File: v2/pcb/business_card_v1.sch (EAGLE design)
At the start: 31 parts, among them SW1 SPST_TACT-KMR2

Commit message: get the led layout right
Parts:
- removed ATTINY: ATTINY45-20X, _hhn_attiny25_45_85:ATTINY45-20X
- removed ISP1: AVRISP-6, adafruit:AVRISP-6
- added IC1: (no value), atmel_tiny24-44-84tiny48-88mega48-88-168-328:ATTINY24/44/84-MU
- added LED21, LED22, LED23, LED24, LED25, LED26, LED27, LED28, LED29, LED30, LED31, LED32, LED33, LED34, LED35, LED36, LED37, LED38, LED39, LED40, LED41, LED42, LED43, LED44, LED45, LED46, LED47, LED48, LED49, LED50, LED51, LED52, LED53, LED54, LED55, LED56: (no value), led:LEDCHIPLED_0805
- added R7, R8, R9: 150, resistor:R-US_R0603
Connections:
- removed net PIN1: ATTINY.PB1, ISP1.MISO, R2.1
- removed net PIN2: ATTINY.PB2, ISP1.SCK, R3.1
- removed net PIN3: ATTINY.PB3, R6.1
- removed net PIN4: ATTINY.PB4, R5.1
- new net N$10: R4.1
- new net N$11: R5.1
- new net N$15: LED10.C, LED11.C, LED12.C, LED13.C, LED14.C, LED15.A, LED23.A, LED31.A, LED39.A, LED47.A, LED55.A, LED7.A, LED8.C, LED9.C, R8.2
- new net N$2: LED10.A, LED18.A, LED2.A, LED26.A, LED34.A, LED42.A, LED43.C, LED44.C, LED45.C, LED46.C, LED47.C, LED48.C, LED49.C, LED50.A, R3.2
- new net N$3: LED11.A, LED19.A, LED27.A, LED3.A, LED35.A, LED36.C, LED37.C, LED38.C, LED39.C, LED40.C, LED41.C, LED42.C, LED43.A, LED51.A, R4.2
- new net N$31: LED14.A, LED15.C, LED16.C, LED17.C, LED18.C, LED19.C, LED20.C, LED21.C, LED22.A, LED30.A, LED38.A, LED46.A, LED54.A, LED6.A, R7.2
- new net N$34: LED13.A, LED21.A, LED22.C, LED23.C, LED24.C, LED25.C, LED26.C, LED27.C, LED28.C, LED29.A, LED37.A, LED45.A, LED5.A, LED53.A, R6.2
- new net N$4: LED12.A, LED20.A, LED28.A, LED29.C, LED30.C, LED31.C, LED32.C, LED33.C, LED34.C, LED35.C, LED36.A, LED4.A, LED44.A, LED52.A, R5.2
- new net N$5: R8.1
- new net N$8: LED1.C, LED16.A, LED2.C, LED24.A, LED3.C, LED32.A, LED4.C, LED40.A, LED48.A, LED5.C, LED56.A, LED6.C, LED7.C, LED8.A, R9.2
- net +5V: no longer ATTINY.VCC, ISP1.VCC
- net GND: no longer ATTINY.GND, ISP1.GND
- net N$1: now also LED17.A, LED25.A, LED33.A, LED41.A, LED49.A, LED50.C, LED51.C, LED52.C, LED53.C, LED54.C, LED55.C, LED56.C, LED9.A; no longer LED11.A, LED16.A, LED17.C, LED18.C, LED19.C, LED20.C, LED6.A
- net N$12: now also R6.1; no longer LED10.C, LED11.C, LED12.C, LED13.A, LED18.A, LED3.A, LED8.A, LED9.C, R4.2
- net N$13: now also R7.1; no longer LED12.A, LED13.C, LED14.C, LED15.C, LED16.C, LED17.A, LED2.A, LED7.A, R3.2
- net N$6: now also R9.1; no longer LED1.C, LED10.A, LED15.A, LED2.C, LED20.A, LED3.C, LED4.C, LED5.A, R6.2
- net N$9: now also R3.1; no longer LED14.A, LED19.A, LED4.A, LED5.C, LED6.C, LED7.C, LED8.C, LED9.A, R5.2
- net PIN0: now also R2.1; no longer ATTINY.PB0, ISP1.MOSI, R4.1
- net RESET: no longer ATTINY.NRES/PB5, ISP1.RST
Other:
- moved on the sheet: C1, JP1, LED1, LED10, LED11, LED12, LED13, LED14, LED15, LED16, LED17, LED18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

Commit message: update pcb and schematic
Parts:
- IC1: device atmel_tiny24-44-84tiny48-88mega48-88-168-328:ATTINY24/44/84-MU -> atmel_tiny24-44-84tiny48-88mega48-88-168-328:ATTINY24/44/84-SSU
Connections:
- net +5V renamed UCC
- removed net N$10: R4.1
- removed net N$11: R5.1
- removed net N$12: R6.1
- removed net N$13: R7.1
- removed net N$5: R8.1
- removed net N$6: R9.1
- removed net N$9: R3.1
- new net PIN1: IC1IC.PA1(ADC1/AIN0/PCINT1), R3.1
- new net PIN2: IC1IC.PA2(ADC2/AIN1/PCINT2), R4.1
- new net PIN3: IC1IC.PA3(ADC3/T0/PCINT3), R5.1
- new net PIN4: IC1IC.PA4(ADC4/USCK/SCL/T1/PCINT4), R6.1
- new net PIN5: IC1IC.PA5(ADC5/MISO/DO/OC1B/PCINT5), R7.1
- new net PIN6: IC1IC.PA6(ADC6/MOSI/SDA/OC1A/PCINT6), R8.1
- new net PIN7: IC1IC.PA7(ADC7/ICP/OC0B/PCINT7), R9.1
- net PIN0: now also IC1IC.PA0(ADC0/AREF/PCINT0)
- net RESET: now also IC1IC.PB3(!RESET!/DW/PCINT11)
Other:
- moved on the sheet: C1, IC1

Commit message: business card
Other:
- moved on the sheet: C1, IC1, JP1, LED1, LED10, LED11, LED12, LED13, LED14, LED15, LED16, LED17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

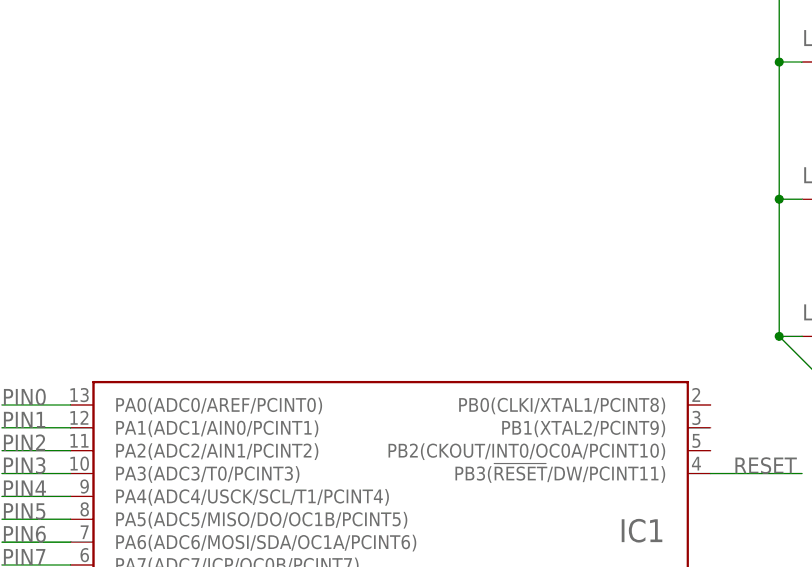
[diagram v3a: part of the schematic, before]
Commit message: get the business card design done, looking for review now
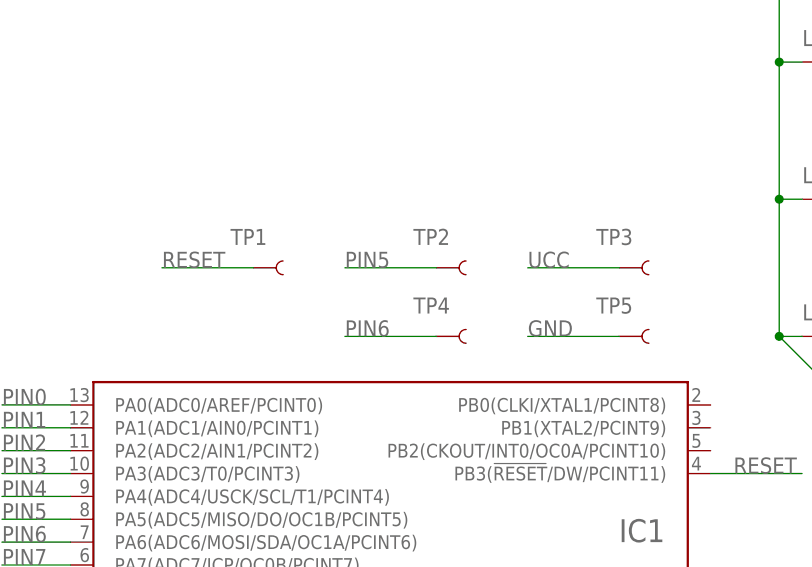
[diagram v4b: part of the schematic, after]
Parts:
- added TP1, TP2, TP3, TP4, TP5: TEST-POINT3X5, SparkFun-Connectors:TEST-POINT3X5
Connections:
- net GND: now also TP5.1
- net PIN5: now also TP2.1
- net PIN6: now also TP4.1
- net RESET: now also TP1.1
- net UCC: now also TP3.1
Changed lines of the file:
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@@
 <layers>
 <layer number="1" name="Top" color="4" fill="1" visible="no" active="no"/>
+<layer number="2" name="Route2" color="1" fill="3" visible="no" active="no"/>
+<layer number="3" name="Route3" color="4" fill="3" visible="no" active="no"/>
+<layer number="4" name="Route4" color="1" fill="4" visible="no" active="no"/>
+<layer number="5" name="Route5" color="4" fill="4" visible="no" active="no"/>
+<layer number="6" name="Route6" color="1" fill="8" visible="no" active="no"/>
+<layer number="7" name="Route7" color="4" fill="8" visible="no" active="no"/>
+<layer number="8" name="Route8" color="1" fill="2" visible="no" active="no"/>
+<layer number="9" name="Route9" color="4" fill="2" visible="no" active="no"/>
+<layer number="10" name="Route10" color="1" fill="7" visible="no" active="no"/>
+<layer number="11" name="Route11" color="4" fill="7" visible="no" active="no"/>
+<layer number="12" name="Route12" color="1" fill="5" visible="no" active="no"/>
+<layer number="13" name="Route13" color="4" fill="5" visible="no" active="no"/>
+<layer number="14" name="Route14" color="1" fill="6" visible="no" active="no"/>
+<layer number="15" name="Route15" color="4" fill="6" visible="no" active="no"/>
 <layer number="16" name="Bottom" color="1" fill="1" visible="no" active="no"/>
 <layer number="17" name="Pads" color="2" fill="1" visible="no" active="no"/>
@@
 <layer number="59" name="tCarbon" color="7" fill="1" visible="no" active="no"/>
 <layer number="60" name="bCarbon" color="7" fill="1" visible="no" active="no"/>
+<layer number="88" name="SimResults" color="9" fill="1" visible="no" active="yes"/>
+<layer number="89" name="SimProbes" color="9" fill="1" visible="no" active="yes"/>
 <layer number="90" name="Modules" color="5" fill="1" visible="yes" active="yes"/>
 <layer number="91" name="Nets" color="2" fill="1" visible="yes" active="yes"/>
@@
 <layer number="112" name="tSilk" color="7" fill="1" visible="no" active="yes"/>
 <layer number="113" name="ReferenceLS" color="7" fill="1" visible="no" active="no"/>
+<layer number="114" name="Badge_Outline" color="7" fill="1" visible="no" active="no"/>
+<layer number="115" name="ReferenceISLANDS" color="7" fill="1" visible="no" active="no"/>
 <layer number="116" name="Patch_BOT" color="9" fill="4" visible="no" active="yes"/>
+<layer number="117" name="PM_Ref" color="7" fill="1" visible="no" active="no"/>
 <layer number="118" name="Rect_Pads" color="7" fill="1" visible="no" active="no"/>
+<layer number="119" name="PF_Ref" color="7" fill="1" visible="no" active="no"/>
+<layer number="120" name="WFL_Ref" color="7" fill="1" visible="no" active="no"/>
 <layer number="121" name="_tsilk" color="7" fill="1" visible="no" active="yes"/>
 <layer number="122" name="_bsilk" color="7" fill="1" visible="no" active="yes"/>
@@
 <part name="IC1" library="atmel_tiny24-44-84tiny48-88mega48-88-168-328" deviceset="ATTINY24/44/84" device="-SSU"/>
 <part name="FRAME1" library="frames" library_urn="urn:adsk.eagle:library:229" deviceset="A4L-LOC" device=""/>
+<part name="TP1" library="SparkFun-Connectors" deviceset="TEST-POINT" device="3X5"/>
+<part name="TP2" library="SparkFun-Connectors" deviceset="TEST-POINT" device="3X5"/>
+<part name="TP3" library="SparkFun-Connectors" deviceset="TEST-POINT" device="3X5"/>
+<part name="TP4" library="SparkFun-Connectors" deviceset="TEST-POINT" device="3X5"/>
+<part name="TP5" library="SparkFun-Connectors" deviceset="TEST-POINT" device="3X5"/>
 </parts>
 <sheets>
@@
 <attribute name="SHEET" x="230.505" y="5.08" size="2.54" layer="94"/>
 </instance>
+<instance part="TP1" gate="G$1" x="38.1" y="76.2" smashed="yes">
+<attribute name="NAME" x="35.56" y="78.74" size="1.778" layer="95" font="vector"/>
+</instance>
+<instance part="TP2" gate="G$1" x="58.42" y="76.2" smashed="yes">
+<attribute name="NAME" x="55.88" y="78.74" size="1.778" layer="95" font="vector"/>
+</instance>
+<instance part="TP3" gate="G$1" x="78.74" y="76.2" smashed="yes">
+<attribute name="NAME" x="76.2" y="78.74" size="1.778" layer="95" font="vector"/>
+</instance>
+<instance part="TP4" gate="G$1" x="58.42" y="68.58" smashed="yes">
+<attribute name="NAME" x="55.88" y="71.12" size="1.778" layer="95" font="vector"/>
+</instance>
+<instance part="TP5" gate="G$1" x="78.74" y="68.58" smashed="yes">
+<attribute name="NAME" x="76.2" y="71.12" size="1.778" layer="95" font="vector"/>
+</instance>
 </instances>
 <busses>
@@
 <junction x="45.72" y="15.24"/>
 </segment>
+<segment>
+<wire x1="38.1" y1="76.2" x2="27.94" y2="76.2" width="0.1524" layer="91"/>
+<label x="27.94" y="76.2" size="1.778" layer="95"/>
+<pinref part="TP1" gate="G$1" pin="1"/>
+</segment>
 </net>
 <net name="GND" class="0">
@@
 <pinref part="GND4" gate="1" pin="GND"/>
 <wire x1="25.4" y1="20.32" x2="25.4" y2="22.86" width="0.1524" layer="91"/>
+</segment>
+<segment>
+<label x="68.58" y="68.58" size="1.778" layer="95"/>
+<pinref part="TP5" gate="G$1" pin="1"/>
+<wire x1="78.74" y1="68.58" x2="68.58" y2="68.58" width="0.1524" layer="91"/>
 </segment>
 </net>
@@
 <pinref part="IC1" gate="IC" pin="PA5(ADC5/MISO/DO/OC1B/PCINT5)"/>
 </segment>
+<segment>
+<wire x1="58.42" y1="76.2" x2="48.26" y2="76.2" width="0.1524" layer="91"/>
+<label x="48.26" y="76.2" size="1.778" layer="95"/>
+<pinref part="TP2" gate="G$1" pin="1"/>
+</segment>
 </net>
 <net name="PIN6" class="0">
@@
 <pinref part="IC1" gate="IC" pin="PA6(ADC6/MOSI/SDA/OC1A/PCINT6)"/>
 </segment>
+<segment>
+<wire x1="58.42" y1="68.58" x2="48.26" y2="68.58" width="0.1524" layer="91"/>
+<label x="48.26" y="68.58" size="1.778" layer="95"/>
+<pinref part="TP4" gate="G$1" pin="1"/>
+</segment>
 </net>
 <net name="PIN7" class="0">
@@
 <label x="45.72" y="33.02" size="1.778" layer="95" rot="R90"/>
 </segment>
+<segment>
+<wire x1="78.74" y1="76.2" x2="68.58" y2="76.2" width="0.1524" layer="91"/>
+<label x="68.58" y="76.2" size="1.778" layer="95"/>
+<pinref part="TP3" gate="G$1" pin="1"/>
+</segment>
 </net>
 </nets>
 </sheet>
 </sheets>
+<errors>
+</errors>
 </schematic>
 </drawing>

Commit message: fix some of the silk screen
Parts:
- TP1, TP2, TP3, TP4, TP5: value TEST-POINT3X5 -> TEST-POINTPOGO_PTH; device SparkFun-Connectors:TEST-POINT3X5 -> SparkFun-Connectors:TEST-POINTPOGO_PTH
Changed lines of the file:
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@@
 <part name="IC1" library="atmel_tiny24-44-84tiny48-88mega48-88-168-328" deviceset="ATTINY24/44/84" device="-SSU"/>
 <part name="FRAME1" library="frames" library_urn="urn:adsk.eagle:library:229" deviceset="A4L-LOC" device=""/>
-<part name="TP1" library="SparkFun-Connectors" deviceset="TEST-POINT" device="3X5"/>
-<part name="TP2" library="SparkFun-Connectors" deviceset="TEST-POINT" device="3X5"/>
-<part name="TP3" library="SparkFun-Connectors" deviceset="TEST-POINT" device="3X5"/>
-<part name="TP4" library="SparkFun-Connectors" deviceset="TEST-POINT" device="3X5"/>
-<part name="TP5" library="SparkFun-Connectors" deviceset="TEST-POINT" device="3X5"/>
+<part name="TP1" library="SparkFun-Connectors" deviceset="TEST-POINT" device="POGO_PTH"/>
+<part name="TP2" library="SparkFun-Connectors" deviceset="TEST-POINT" device="POGO_PTH"/>
+<part name="TP3" library="SparkFun-Connectors" deviceset="TEST-POINT" device="POGO_PTH"/>
+<part name="TP4" library="SparkFun-Connectors" deviceset="TEST-POINT" device="POGO_PTH"/>
+<part name="TP5" library="SparkFun-Connectors" deviceset="TEST-POINT" device="POGO_PTH"/>
 </parts>
 <sheets>
@@
 <segment>
 <label x="68.58" y="68.58" size="1.778" layer="95"/>
+<wire x1="78.74" y1="68.58" x2="68.58" y2="68.58" width="0.1524" layer="91"/>
 <pinref part="TP5" gate="G$1" pin="1"/>
-<wire x1="78.74" y1="68.58" x2="68.58" y2="68.58" width="0.1524" layer="91"/>
 </segment>
 </net>
@@
 </sheet>
 </sheets>
-<errors>
-</errors>
 </schematic>
 </drawing>
